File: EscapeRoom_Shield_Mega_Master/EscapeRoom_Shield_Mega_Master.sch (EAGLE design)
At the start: 73 parts

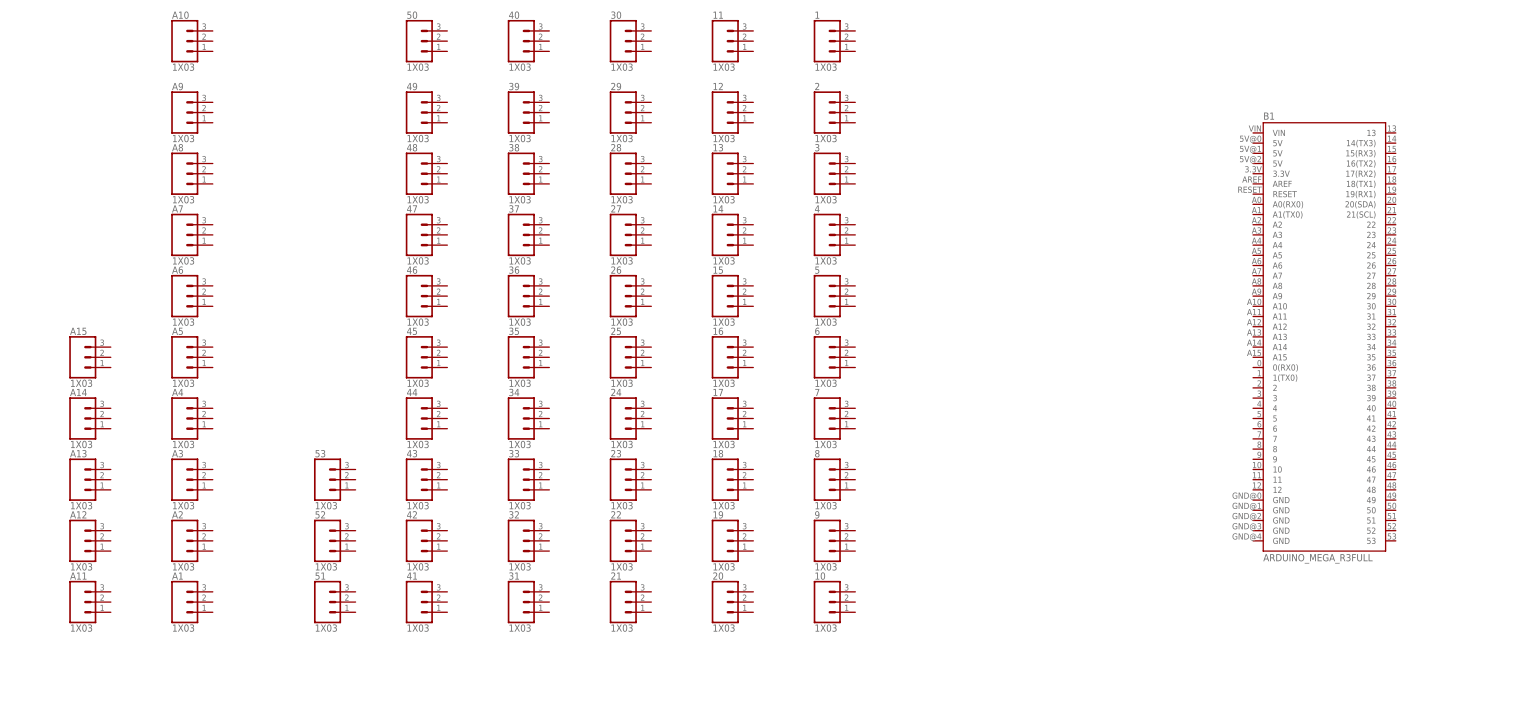
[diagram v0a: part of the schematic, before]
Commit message: Finished defining pin breakouts, wiring pins
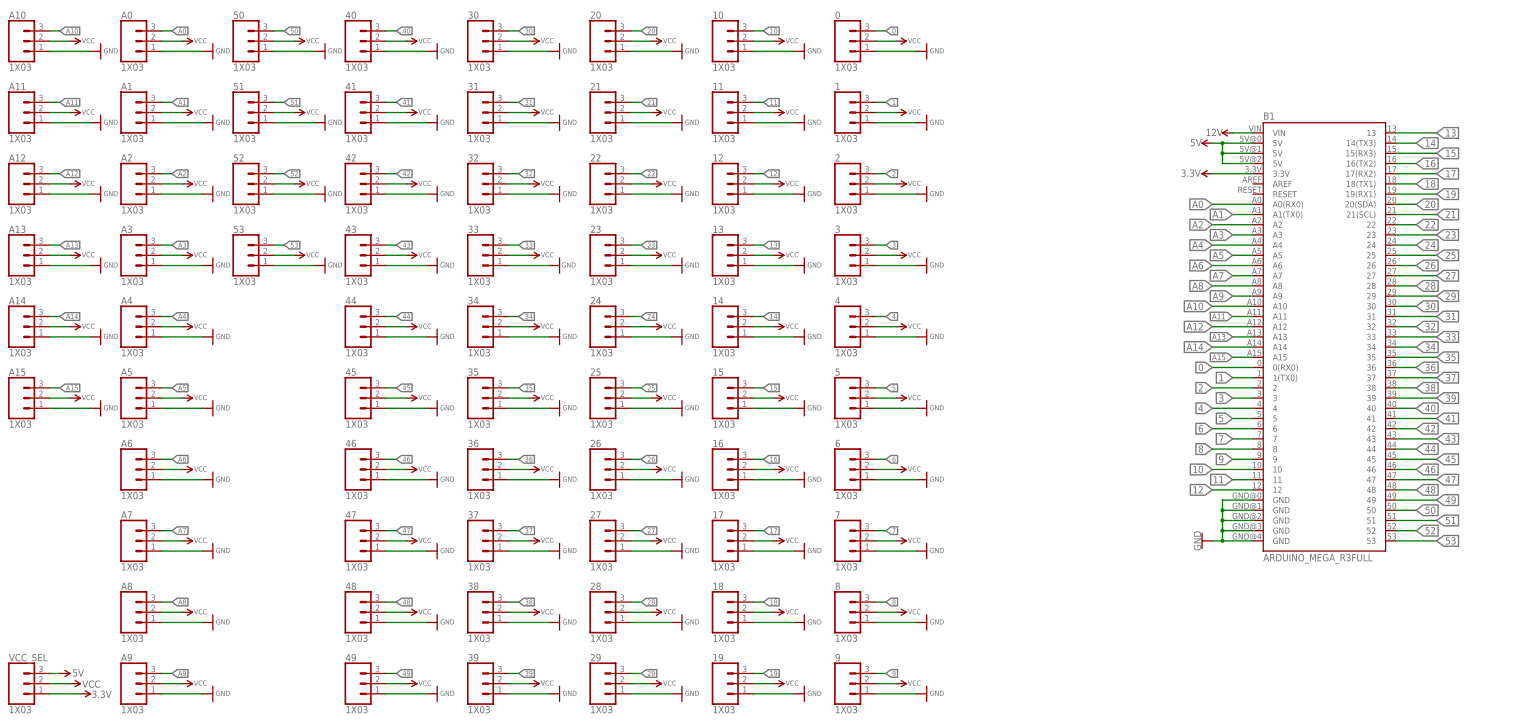
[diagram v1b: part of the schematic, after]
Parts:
- added 0, A0, VCC_SEL: 1X03, Adam's Parts (work):1X03
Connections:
- new net 0: 0.3, B1.0(RX0)
- new net 1: 1.3, B1.1(TX0)
- new net 10: 10.3, B1.10
- new net 11: 11.3, B1.11
- new net 12: 12.3, B1.12
- new net 12V: B1.VIN
- new net 13: 13.3, B1.13
- new net 14: 14.3, B1.14(TX3)
- new net 15: 15.3, B1.15(RX3)
- new net 16: 16.3, B1.16(TX2)
- new net 17: 17.3, B1.17(RX2)
- new net 18: 18.3, B1.18(TX1)
- new net 19: 19.3, B1.19(RX1)
- new net 2: 2.3, B1.2
- new net 20: 20.3, B1.20(SDA)
- new net 21: 21.3, B1.21(SCL)
- new net 22: 22.3, B1.22
- new net 23: 23.3, B1.23
- new net 24: 24.3, B1.24
- new net 25: 25.3, B1.25
- new net 26: 26.3, B1.26
- new net 27: 27.3, B1.27
- new net 28: 28.3, B1.28
- new net 29: 29.3, B1.29
- new net 3: 3.3, B1.3
- new net 3.3V: B1.3.3V, VCC_SEL.1
- new net 30: 30.3, B1.30
- new net 31: 31.3, B1.31
- new net 32: 32.3, B1.32
- new net 33: 33.3, B1.33
- new net 34: 34.3, B1.34
- new net 35: 35.3, B1.35
- new net 36: 36.3, B1.36
- new net 37: 37.3, B1.37
- new net 38: 38.3, B1.38
- new net 39: 39.3, B1.39
- new net 4: 4.3, B1.4
- new net 40: 40.3, B1.40
- new net 41: 41.3, B1.41
- new net 42: 42.3, B1.42
- new net 43: 43.3, B1.43
- new net 44: 44.3, B1.44
- new net 45: 45.3, B1.45
- new net 46: 46.3, B1.46
- new net 47: 47.3, B1.47
- new net 48: 48.3, B1.48
- new net 49: 49.3, B1.49
- new net 5: 5.3, B1.5
- new net 50: 50.3, B1.50
- new net 51: 51.3, B1.51
- new net 52: 52.3, B1.52
- new net 53: 53.3, B1.53
- new net 5V: B1.5V@0, B1.5V@1, B1.5V@2, VCC_SEL.3
- new net 6: 6.3, B1.6
- new net 7: 7.3, B1.7
- new net 8: 8.3, B1.8
- new net 9: 9.3, B1.9
- new net A0: A0.3, B1.A0(RX0)
- new net A1: A1.3, B1.A1(TX0)
- new net A10: A10.3, B1.A10
- new net A11: A11.3, B1.A11
- new net A12: A12.3, B1.A12
- new net A13: A13.3, B1.A13
- new net A14: A14.3, B1.A14
- new net A15: A15.3, B1.A15
- new net A2: A2.3, B1.A2
- new net A3: A3.3, B1.A3
- new net A4: A4.3, B1.A4
- new net A5: A5.3, B1.A5
- new net A6: A6.3, B1.A6
- new net A7: A7.3, B1.A7
- new net A8: A8.3, B1.A8
- new net A9: A9.3, B1.A9
- new net GND: 0.1, 1.1, 10.1, 11.1, 12.1, 13.1, 14.1, 15.1, 16.1, 17.1, 18.1, 19.1, 2.1, 20.1, 21.1, 22.1, 23.1, 24.1, 25.1, 26.1, 27.1, 28.1, 29.1, 3.1, 30.1, 31.1, 32.1, 33.1, 34.1, 35.1, 36.1, 37.1, 38.1, 39.1, 4.1, 40.1, 41.1, 42.1, 43.1, 44.1, 45.1, 46.1, 47.1, 48.1, 49.1, 5.1, 50.1, 51.1, 52.1, 53.1, 6.1, 7.1, 8.1, 9.1, A0.1, A1.1, A10.1, A11.1, A12.1, A13.1, A14.1, A15.1, A2.1, A3.1, A4.1, A5.1, A6.1, A7.1, A8.1, A9.1, B1.GND@0, B1.GND@1, B1.GND@2, B1.GND@3, B1.GND@4
- new net VCC: 0.2, 1.2, 10.2, 11.2, 12.2, 13.2, 14.2, 15.2, 16.2, 17.2, 18.2, 19.2, 2.2, 20.2, 21.2, 22.2, 23.2, 24.2, 25.2, 26.2, 27.2, 28.2, 29.2, 3.2, 30.2, 31.2, 32.2, 33.2, 34.2, 35.2, 36.2, 37.2, 38.2, 39.2, 4.2, 40.2, 41.2, 42.2, 43.2, 44.2, 45.2, 46.2, 47.2, 48.2, 49.2, 5.2, 50.2, 51.2, 52.2, 53.2, 6.2, 7.2, 8.2, 9.2, A0.2, A1.2, A10.2, A11.2, A12.2, A13.2, A14.2, A15.2, A2.2, A3.2, A4.2, A5.2, A6.2, A7.2, A8.2, A9.2, VCC_SEL.2
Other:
- moved on the sheet: 1, 10, 11, 12, 13, 14, 15, 16, 17, 18, 19, 2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

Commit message: Changed DFMini TX/RX pins to compatible pins. Removed R1. Labeled 12V out terminal blocks.
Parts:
- removed VCC_SEL: 1X03, Adam's Parts (work):1X03
- added JP1: JUMPER-SMT_3_1-NC_TRACE_SILK, SparkFun-Jumpers:JUMPER-SMT_3_1-NC_TRACE_SILK
- added U$5, U$7, U$8, U$9: TERMINAL_BLOCK_2P, Adam's Parts (work):TERMINAL_BLOCK_2P
- added U$6: BUTTON_PTS636_SL50_LFS, Adam's Parts (work):BUTTON_PTS636_SL50_LFS
- renumbered 12 to 12*, 13 to 13*, 20 to 20*, 21 to 21*, 22 to 22*
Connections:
- new net N$1: U$2.COM, U$4.P$2
- new net N$2: U$2.NO, U$4.P$1
- new net N$3: U$2.NC, U$4.P$3
- new net N$5: U$3.P$16, U$5.1
- new net N$6: U$3.P$14, U$5.2
- new net N$7: B1.RESET, U$6.B
- net 12: now also U$3.P$11
- net 12V: now also U$1.1, U$7.1, U$8.1, U$9.1
- net 13: now also U$3.P$10
- net 20: now also U$1.2
- net 21: now also U$1.3
- net 22: now also U$2.V+
- net 3.3V: now also JP1.1; no longer VCC_SEL.1
- net 5V: now also JP1.3, U$3.P$9; no longer VCC_SEL.3
- net GND: now also U$1.8, U$1.SHIELD1, U$1.SHIELD2, U$2.V-, U$3.P$15, U$3.P$7, U$6.A1, U$7.2, U$8.2, U$9.2
- net VCC: now also JP1.2; no longer VCC_SEL.2
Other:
- moved on the sheet: U$4
